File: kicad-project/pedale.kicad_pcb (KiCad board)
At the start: 2 copper layers, 121.5 x 81.5 mm, 10 parts

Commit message: modificari dupa sugestii
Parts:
- removed U9: ~, Connector_PinHeader_2.54mm:PinHeader_1x01_P2.54mm_Vertical
- moved U1 104.2 mm to (27.0, 78.0), turned to 0 degrees
- moved U8 103.5 mm to (27.0, 67.0), turned to 0 degrees
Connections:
- J1 pad 11: GND -> unconnected-(J1-GND-Pad11)
- J13 pad 14: GND -> unconnected-(J13-GND-Pad14)
- J13 pad 2: unconnected-(J13-VBAT-Pad2) -> 12V
- J2 pad 7: GND -> unconnected-(J2-GND-Pad7)
- J4 pad 10: GND -> unconnected-(J4-GND-Pad10)
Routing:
- net /CAN_P: track 108.8 -> 4.46 mm
- net /CAN_N: track 100.3 -> 4.48 mm
- net 12V: track 83.4 -> 29.2 mm
- net GND: vias 14 -> 0

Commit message: modificari 2
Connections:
- J13 pad 1: unconnected-(J13-ptc25-Pad1) -> 12V
- J13 pad 11: unconnected-(J13-ptd21-Pad11) -> GND
- J13 pad 12: GND -> unconnected-(J13-ptd21-Pad12)
- J13 pad 2: 12V -> unconnected-(J13-ptc25-Pad2)
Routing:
- net 12V: track 29.2 -> 28.1 mm
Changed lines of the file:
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@@
 	(net 0 "")
 	(net 1 "GND")
-	(net 2 "unconnected-(J13-RESET-Pad6)")
-	(net 3 "unconnected-(J13-+3.3V-Pad8)")
-	(net 4 "unconnected-(J13-ptd21-Pad11)")
-	(net 5 "unconnected-(J13-ptd20-Pad9)")
-	(net 6 "unconnected-(J13-+5V-Pad10)")
-	(net 7 "unconnected-(J13-ptc25-Pad1)")
-	(net 8 "unconnected-(J13-VBAT-Pad16)")
-	(net 9 "unconnected-(J13-ptc30-Pad13)")
-	(net 10 "unconnected-(J13-VDD-Pad4)")
-	(net 11 "unconnected-(J13-ptc31-Pad15)")
+	(net 2 "unconnected-(J13-pta29-Pad6)")
+	(net 3 "unconnected-(J13-ptb11-Pad8)")
+	(net 4 "unconnected-(J13-+5V-Pad9)")
+	(net 5 "unconnected-(J13-ptd20-Pad10)")
+	(net 6 "unconnected-(J13-ptc31-Pad16)")
+	(net 7 "unconnected-(J13-ptd21-Pad12)")
+	(net 8 "unconnected-(J13-GND-Pad13)")
+	(net 9 "unconnected-(J13-ptc24-Pad4)")
+	(net 10 "unconnected-(J13-ptc30-Pad14)")
+	(net 11 "unconnected-(J13-VBAT-Pad15)")
 	(net 12 "unconnected-(J1-GND-Pad11)")
-	(net 13 "unconnected-(J13-ptc24-Pad3)")
-	(net 14 "unconnected-(J13-ptb11-Pad7)")
-	(net 15 "unconnected-(J13-pta29-Pad5)")
+	(net 13 "unconnected-(J13-ptc25-Pad2)")
+	(net 14 "unconnected-(J13-VDD-Pad3)")
+	(net 15 "unconnected-(J13-+3.3V-Pad7)")
 	(net 16 "unconnected-(J14-pta28-Pad15)")
 	(net 17 "unconnected-(J14-ptc13-Pad11)")
@@
 	(net 110 "unconnected-(J2-GND-Pad7)")
 	(net 111 "unconnected-(J4-GND-Pad10)")
-	(net 112 "unconnected-(J13-GND-Pad14)")
+	(net 112 "unconnected-(J13-RESET-Pad5)")
 	(footprint "Connector_PinSocket_2.00mm:PinSocket_1x02_P2.00mm_Horizontal"
 		(layer "F.Cu")
@@
 			(layers "*.Cu" "*.Mask")
 			(remove_unused_layers no)
-			(net 7 "unconnected-(J13-ptc25-Pad1)")
-			(pinfunction "ptc25")
-			(pintype "passive+no_connect")
+			(net 102 "12V")
+			(pinfunction "VBAT")
+			(pintype "passive")
 		)
 		(pad "2" thru_hole circle
@@
 			(layers "*.Cu" "*.Mask")
 			(remove_unused_layers no)
-			(net 102 "12V")
-			(pinfunction "VBAT")
-			(pintype "passive")
+			(net 13 "unconnected-(J13-ptc25-Pad2)")
+			(pinfunction "ptc25")
+			(pintype "passive+no_connect")
 		)
 		(pad "3" thru_hole circle
@@
 			(layers "*.Cu" "*.Mask")
 			(remove_unused_layers no)
-			(net 13 "unconnected-(J13-ptc24-Pad3)")
-			(pinfunction "ptc24")
+			(net 14 "unconnected-(J13-VDD-Pad3)")
+			(pinfunction "VDD")
 			(pintype "passive+no_connect")
 		)
@@
 			(layers "*.Cu" "*.Mask")
 			(remove_unused_layers no)
-			(net 10 "unconnected-(J13-VDD-Pad4)")
-			(pinfunction "VDD")
+			(net 9 "unconnected-(J13-ptc24-Pad4)")
+			(pinfunction "ptc24")
 			(pintype "passive+no_connect")
 		)
@@
 			(layers "*.Cu" "*.Mask")
 			(remove_unused_layers no)
-			(net 15 "unconnected-(J13-pta29-Pad5)")
-			(pinfunction "pta29")
+			(net 112 "unconnected-(J13-RESET-Pad5)")
+			(pinfunction "RESET")
 			(pintype "passive+no_connect")
 		)
@@
 			(layers "*.Cu" "*.Mask")
 			(remove_unused_layers no)
-			(net 2 "unconnected-(J13-RESET-Pad6)")
-			(pinfunction "RESET")
+			(net 2 "unconnected-(J13-pta29-Pad6)")
+			(pinfunction "pta29")
 			(pintype "passive+no_connect")
 		)
@@
 			(layers "*.Cu" "*.Mask")
 			(remove_unused_layers no)
-			(net 14 "unconnected-(J13-ptb11-Pad7)")
-			(pinfunction "ptb11")
+			(net 15 "unconnected-(J13-+3.3V-Pad7)")
+			(pinfunction "+3.3V")
 			(pintype "passive+no_connect")
 		)
@@
 			(layers "*.Cu" "*.Mask")
 			(remove_unused_layers no)
-			(net 3 "unconnected-(J13-+3.3V-Pad8)")
-			(pinfunction "+3.3V")
+			(net 3 "unconnected-(J13-ptb11-Pad8)")
+			(pinfunction "ptb11")
 			(pintype "passive+no_connect")
 		)
@@
 			(layers "*.Cu" "*.Mask")
 			(remove_unused_layers no)
-			(net 5 "unconnected-(J13-ptd20-Pad9)")
-			(pinfunction "ptd20")
+			(net 4 "unconnected-(J13-+5V-Pad9)")
+			(pinfunction "+5V")
 			(pintype "passive+no_connect")
 		)
@@
 			(layers "*.Cu" "*.Mask")
 			(remove_unused_layers no)
-			(net 6 "unconnected-(J13-+5V-Pad10)")
-			(pinfunction "+5V")
+			(net 5 "unconnected-(J13-ptd20-Pad10)")
+			(pinfunction "ptd20")
 			(pintype "passive+no_connect")
 		)
@@
 			(layers "*.Cu" "*.Mask")
 			(remove_unused_layers no)
-			(net 4 "unconnected-(J13-ptd21-Pad11)")
-			(pinfunction "ptd21")
-			(pintype "passive+no_connect")
+			(net 1 "GND")
+			(pinfunction "GND")
+			(pintype "passive")
 		)
 		(pad "12" thru_hole circle
@@
 			(layers "*.Cu" "*.Mask")
 			(remove_unused_layers no)
-			(net 1 "GND")
-			(pinfunction "GND")
-			(pintype "passive")
+			(net 7 "unconnected-(J13-ptd21-Pad12)")
+			(pinfunction "ptd21")
+			(pintype "passive+no_connect")
 		)
 		(pad "13" thru_hole circle
@@
 			(layers "*.Cu" "*.Mask")
 			(remove_unused_layers no)
-			(net 9 "unconnected-(J13-ptc30-Pad13)")
-			(pinfunction "ptc30")
+			(net 8 "unconnected-(J13-GND-Pad13)")
+			(pinfunction "GND")
 			(pintype "passive+no_connect")
 		)
@@
 			(layers "*.Cu" "*.Mask")
 			(remove_unused_layers no)
-			(net 112 "unconnected-(J13-GND-Pad14)")
-			(pinfunction "GND")
+			(net 10 "unconnected-(J13-ptc30-Pad14)")
+			(pinfunction "ptc30")
 			(pintype "passive+no_connect")
 		)
@@
 			(layers "*.Cu" "*.Mask")
 			(remove_unused_layers no)
-			(net 11 "unconnected-(J13-ptc31-Pad15)")
-			(pinfunction "ptc31")
+			(net 11 "unconnected-(J13-VBAT-Pad15)")
+			(pinfunction "VBAT")
 			(pintype "passive+no_connect")
 		)
@@
 			(layers "*.Cu" "*.Mask")
 			(remove_unused_layers no)
-			(net 8 "unconnected-(J13-VBAT-Pad16)")
-			(pinfunction "VBAT")
+			(net 6 "unconnected-(J13-ptc31-Pad16)")
+			(pinfunction "ptc31")
 			(pintype "passive+no_connect")
 		)
@@
 	)
 	(segment
-		(start 38.8 88)
+		(start 36.26 85.46)
 		(end 30.8 80)
 		(width 1)
@@
 	)
 	(segment
-		(start 52.88 88)
-		(end 38.8 88)
+		(start 52.88 85.46)
+		(end 36.26 85.46)
 		(width 1)
 		(layer "B.Cu")
@@
 		(polygon
 			(pts
-				(xy 109 87.5) (xy 113.5 87.5) (xy 113.5 86) (xy 109 86)
+				(xy 64 87.5) (xy 68.5 87.5) (xy 68.5 86) (xy 64 86)
 			)
 		)

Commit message: viorel approved
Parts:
- added D1: SS32, Diode_SMD:D_SMA, F.Cu at (34.5, 78.0)
- U1, U8: footprint Connector_PinSocket_2.00mm:PinSocket_1x02_P2.00mm_Horizontal -> Connector_JST:JST_PH_B2B-PH-K_1x02_P2.00mm_Vertical
- moved U1 0.71 mm to (26.5, 77.5), turned to -90 degrees
- moved U8 0.50 mm to (26.5, 67.0), turned to -90 degrees
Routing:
- net 12V: track 28.1 -> 30.7 mm
- net /CAN_P: track 4.46 -> 4.96 mm
- net /CAN_N: track 4.48 -> 4.98 mm
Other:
- board size 121.5 x 81.5 mm -> 114 x 70.5 mm

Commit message: corectat footprint dioda
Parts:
- D1: footprint Diode_SMD:D_SMA -> Diode_SMD:D_SMB
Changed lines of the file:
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@@
 	(net 111 "unconnected-(J4-GND-Pad10)")
 	(net 112 "unconnected-(J13-RESET-Pad5)")
-	(footprint "Diode_SMD:D_SMA"
+	(footprint "Diode_SMD:D_SMB"
 		(layer "F.Cu")
 		(at 34.5 78 90)
-		(descr "Diode SMA (DO-214AC)")
-		(tags "Diode SMA (DO-214AC)")
+		(descr "Diode SMB (DO-214AA)")
+		(tags "Diode SMB (DO-214AA)")
 		(property "Reference" "D1"
-			(at 0 -2.5 90)
+			(at 0 -3 90)
 			(layer "F.SilkS")
 			(effects
@@
 		)
 		(property "Value" "SS32"
-			(at 0 2.6 90)
+			(at 0 3.1 90)
 			(layer "F.Fab")
 			(effects
@@
 		(attr smd)
 		(fp_line
-			(start -3.51 -1.65)
-			(end 2 -1.65)
+			(start -3.66 -2.15)
+			(end 2.15 -2.15)
 			(stroke
 				(width 0.12)
@@
 		)
 		(fp_line
-			(start -3.51 -1.65)
-			(end -3.51 1.65)
+			(start -3.66 -2.15)
+			(end -3.66 2.15)
 			(stroke
 				(width 0.12)
@@
 		)
 		(fp_line
-			(start -3.51 1.65)
-			(end 2 1.65)
+			(start -3.66 2.15)
+			(end 2.15 2.15)
 			(stroke
 				(width 0.12)
@@
 		)
 		(fp_line
-			(start 3.5 -1.75)
-			(end 3.5 1.75)
+			(start 3.65 -2.25)
+			(end 3.65 2.25)
 			(stroke
 				(width 0.05)
@@
 		)
 		(fp_line
-			(start -3.5 -1.75)
-			(end 3.5 -1.75)
+			(start -3.65 -2.25)
+			(end 3.65 -2.25)
 			(stroke
 				(width 0.05)
@@
 		)
 		(fp_line
-			(start 3.5 1.75)
-			(end -3.5 1.75)
+			(start 3.65 2.25)
+			(end -3.65 2.25)
 			(stroke
 				(width 0.05)
@@
 		)
 		(fp_line
-			(start -3.5 1.75)
-			(end -3.5 -1.75)
+			(start -3.65 2.25)
+			(end -3.65 -2.25)
 			(stroke
 				(width 0.05)
@@
 		)
 		(fp_line
-			(start 2.3 -1.5)
-			(end -2.3 -1.5)
+			(start 2.3 -2)
+			(end -2.3 -2)
 			(stroke
 				(width 0.1)
@@
 		)
 		(fp_line
-			(start 2.3 -1.5)
-			(end 2.3 1.5)
+			(start 2.3 -2)
+			(end 2.3 2)
 			(stroke
 				(width 0.1)
@@
 		)
 		(fp_line
-			(start 2.3 1.5)
-			(end -2.3 1.5)
+			(start 2.3 2)
+			(end -2.3 2)
 			(stroke
 				(width 0.1)
@@
 		)
 		(fp_line
-			(start -2.3 1.5)
-			(end -2.3 -1.5)
+			(start -2.3 2)
+			(end -2.3 -2)
 			(stroke
 				(width 0.1)
@@
 		)
 		(fp_text user "${REFERENCE}"
-			(at 0 -2.5 90)
+			(at 0 -3 90)
 			(layer "F.Fab")
 			(effects
@@
 		)
 		(pad "1" smd roundrect
-			(at -2 0 90)
-			(size 2.5 1.8)
+			(at -2.15 0 90)
+			(size 2.5 2.3)
 			(layers "F.Cu" "F.Mask" "F.Paste")
-			(roundrect_rratio 0.1388888889)
+			(roundrect_rratio 0.1086956522)
 			(net 102 "12V")
 			(pinfunction "K")
@@
 		)
 		(pad "2" smd roundrect
-			(at 2 0 90)
-			(size 2.5 1.8)
+			(at 2.15 0 90)
+			(size 2.5 2.3)
 			(layers "F.Cu" "F.Mask" "F.Paste")
-			(roundrect_rratio 0.1388888889)
+			(roundrect_rratio 0.1086956522)
 			(net 1 "GND")
 			(pinfunction "A")
@@
 		)
 		(embedded_fonts no)
-		(model "${KICAD9_3DMODEL_DIR}/Diode_SMD.3dshapes/D_SMA.step"
+		(model "${KICAD9_3DMODEL_DIR}/Diode_SMD.3dshapes/D_SMB.step"
 			(offset
 				(xyz 0 0 0)
@@
 	)
 	(segment
+		(start 34.5 80.15)
+		(end 34.35 80)
+		(width 1)
+		(layer "F.Cu")
+		(net 102)
+	)
+	(segment
+		(start 52.88 85.46)
+		(end 52.88 82.38)
+		(width 1)
+		(layer "F.Cu")
+		(net 102)
+	)
+	(segment
 		(start 27 80)
 		(end 26.5 79.5)
@@
 	)
 	(segment
-		(start 50.5 80)
-		(end 32 80)
+		(start 34.65 80)
+		(end 34.5 80.15)
 		(width 1)
 		(layer "F.Cu")
@@
 	)
 	(segment
-		(start 32 80)
-		(end 27 80)
+		(start 50.5 80)
+		(end 34.65 80)
 		(width 1)
 		(layer "F.Cu")
@@
 	)
 	(segment
-		(start 52.88 82.38)
-		(end 50.5 80)
+		(start 34.35 80)
+		(end 27 80)
 		(width 1)
 		(layer "F.Cu")
@@
 	)
 	(segment
-		(start 52.88 85.46)
-		(end 52.88 82.38)
+		(start 52.88 82.38)
+		(end 50.5 80)
 		(width 1)
 		(layer "F.Cu")

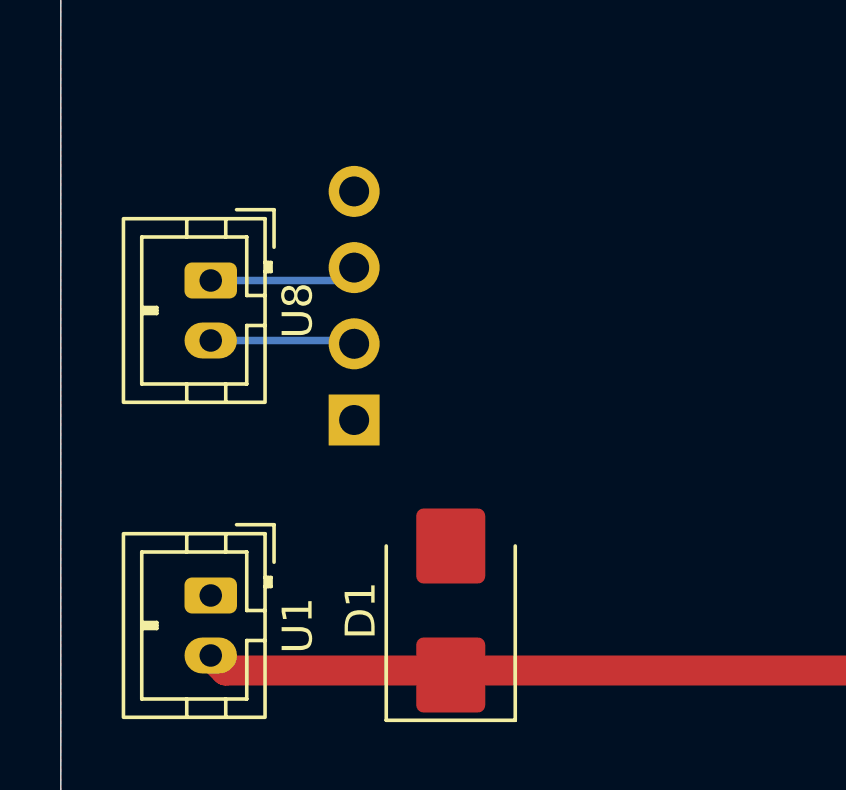
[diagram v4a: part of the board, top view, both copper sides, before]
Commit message: CAN_IN & CAN_OUT - added
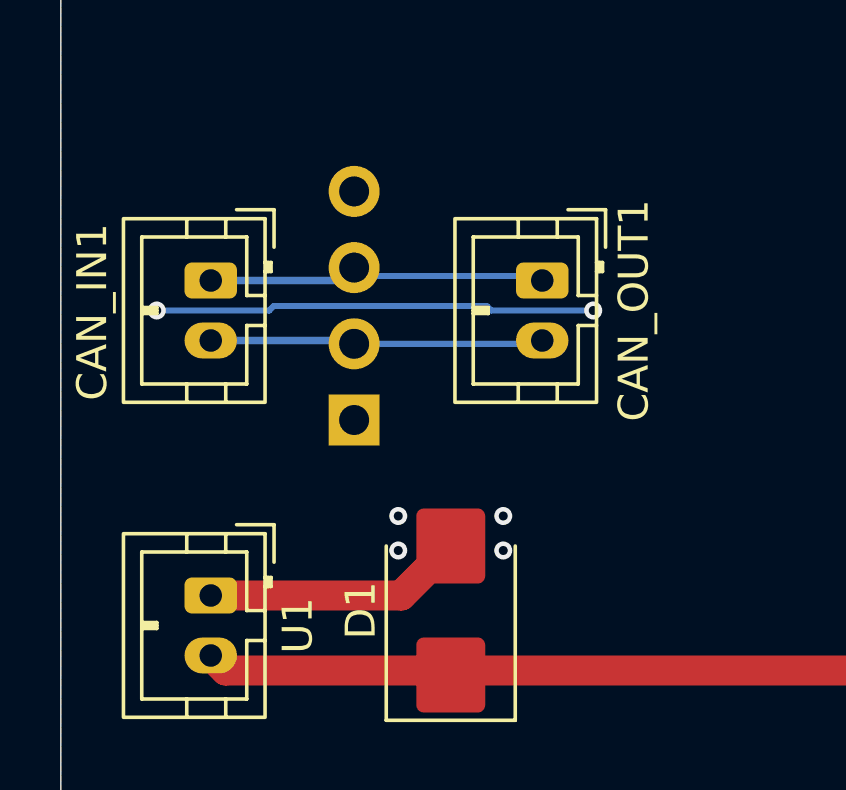
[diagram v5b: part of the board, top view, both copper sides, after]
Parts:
- added CAN_OUT1: ~, Connector_JST:JST_PH_B2B-PH-K_1x02_P2.00mm_Vertical, F.Cu at (37.5, 67.0)
- renumbered U8 to CAN_IN1
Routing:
- net GND: track 0.00 -> 23.4 mm, vias 0 -> 6
- net /CAN_P: track 4.96 -> 11.4 mm
- net /CAN_N: track 4.98 -> 11.3 mm
